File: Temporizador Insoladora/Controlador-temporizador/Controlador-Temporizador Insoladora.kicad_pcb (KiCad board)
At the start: 2 copper layers, 170.2 x 96.5 mm, 72 parts, among them P1 ICSP, P2 CONN_01X03, P3 CARGA, P4 TRANSF, P5 VAC, P7 CONN_02X08, Q1 BC548, Q2 BC548, Q3 BC548, Q4 BC548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

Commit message: Acomodando el controlador
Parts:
- P2: value CONN_01X03 -> VAC12V
- moved D2 161.8 mm to (48.3, 69.8)
- moved D3 161.8 mm to (48.3, 64.8)
- moved P4 157.3 mm to (199.4, 87.6), turned to 270 degrees
- moved P5 145.4 mm to (199.4, 74.9), turned to 270 degrees
- moved P2 131.4 mm to (64.8, 73.7)
- moved F1 130.1 mm to (186.7, 77.5), turned to 90 degrees
- moved VR1 122.3 mm to (193.0, 82.5), turned to 90 degrees
- moved R10 76.0 mm to (52.1, 123.2)
- moved R11 76.0 mm to (50.8, 128.3)
- moved P7 71.1 mm to (134.6, 147.3), turned to 180 degrees
- moved Q6 69.1 mm to (109.2, 141.0), turned to 90 degrees
- moved R29 64.3 mm to (105.4, 134.6), turned to 90 degrees
- moved Q3 64.3 mm to (143.5, 139.7), turned to 90 degrees
- moved Q5 64.2 mm to (118.1, 141.0), turned to 90 degrees
- moved R15 62.6 mm to (151.1, 86.4), turned to 90 degrees
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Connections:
- P1 pad 6: Net-(P1-Pad6) -> (no net)
- P5 pad 2: Earth -> (no net)
- P7 pad 11: Net-(P7-Pad11) -> (no net)
- P7 pad 5: Net-(P7-Pad5) -> (no net)
- P7 pad 7: Net-(P7-Pad7) -> (no net)
- P7 pad 9: Net-(P7-Pad9) -> (no net)
- U2 pad 10: Net-(U2-Pad10) -> (no net)
- U2 pad 2: Net-(U2-Pad2) -> (no net)
- U2 pad 24: Net-(U2-Pad24) -> (no net)
- U2 pad 25: Net-(U2-Pad25) -> (no net)
- U2 pad 26: Net-(U2-Pad26) -> (no net)
- U2 pad 3: Net-(U2-Pad3) -> (no net)
- U2 pad 34: Net-(U2-Pad34) -> (no net)
- U2 pad 4: Net-(U2-Pad4) -> (no net)
- U2 pad 5: Net-(U2-Pad5) -> (no net)
- U2 pad 6: Net-(U2-Pad6) -> (no net)
- U2 pad 7: Net-(U2-Pad7) -> (no net)
- U2 pad 8: Net-(U2-Pad8) -> (no net)
- U2 pad 9: Net-(U2-Pad9) -> (no net)
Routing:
- net Net-(C13-Pad2): track 0.00 -> 48.2 mm
- net Net-(P3-Pad2): track 0.00 -> 36.4 mm
- net Net-(F1-Pad1): track 0.00 -> 34.8 mm
- net Net-(R19-Pad1): track 0.00 -> 16.6 mm
- net Net-(F1-Pad2): track 0.00 -> 15.2 mm
- net /D: track 22.1 -> 8.89 mm
- net SEGUKC: track 10.5 -> 0.00 mm
- net Net-(Q1-Pad2): track 0.00 -> 8.67 mm
- net Net-(R15-Pad1): track 0.00 -> 5.68 mm
- net Net-(R18-Pad2): track 0.00 -> 5.16 mm
- net SEGDKC: track 4.86 -> 0.00 mm
- net Net-(Q1-Pad1): track 0.00 -> 3.81 mm
- net Net-(Q5-Pad2): track 3.81 -> 0.00 mm
- net Net-(C13-Pad1): track 0.00 -> 3.59 mm
- net /E: track 6.35 -> 8.89 mm
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
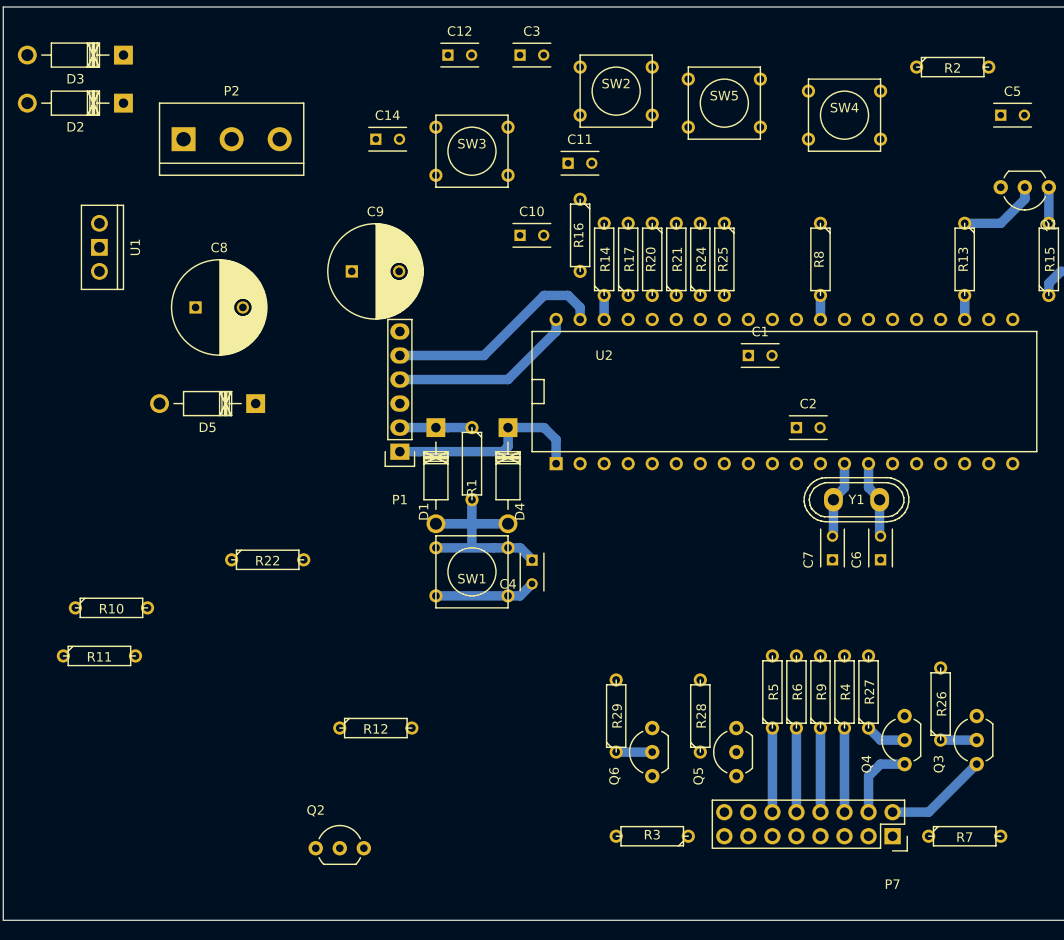
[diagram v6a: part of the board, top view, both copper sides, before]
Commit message: Ruteando controlador
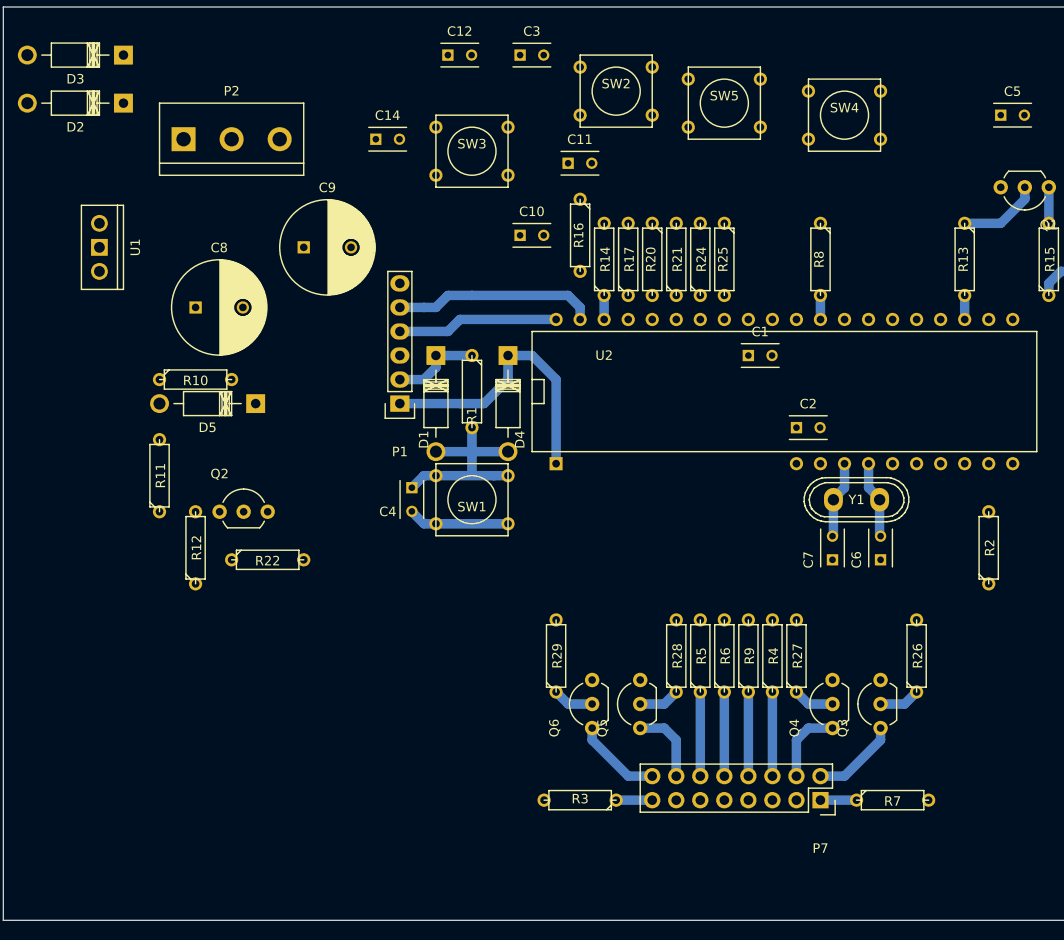
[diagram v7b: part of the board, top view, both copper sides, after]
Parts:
- moved R2 50.9 mm to (144.8, 116.8), turned to 90 degrees
- moved Q2 37.0 mm to (63.5, 113.0)
- moved R12 26.9 mm to (61.0, 116.8), turned to 90 degrees
- moved R10 25.7 mm to (61.0, 99.1)
- moved R11 20.1 mm to (57.1, 109.2), turned to 90 degrees
- moved C4 14.8 mm to (83.8, 110.5)
- moved Q5 11.4 mm to (108.0, 135.9)
- moved Q3 10.9 mm to (133.3, 135.9)
- moved R29 8.98 mm to (99.1, 128.3)
- moved R27 8.52 mm to (124.5, 128.3)
- moved P7 8.52 mm to (127.0, 143.5)
- moved R3 8.52 mm to (101.6, 143.5)
- moved R5 8.52 mm to (114.3, 128.3)
- moved R7 8.52 mm to (134.6, 143.5)
- moved R9 8.52 mm to (119.4, 128.3)
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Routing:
- net SEGUKC: track 0.00 -> 9.20 mm
- net ~MCLR~/VPP: track 21.8 -> 30.0 mm
- net SEGDKC: track 0.00 -> 8.15 mm
- net Net-(Q5-Pad2): track 0.00 -> 4.34 mm
- net /F: track 0.00 -> 3.81 mm
- net /B: track 0.00 -> 3.81 mm
- net PGD: track 19.9 -> 17.0 mm
- net PGC: track 23.5 -> 21.4 mm
- net VCC: track 7.62 -> 9.42 mm
- net MINDKC: track 11.0 -> 9.20 mm
- net Net-(Q6-Pad2): track 3.81 -> 4.34 mm
- net Net-(Q3-Pad2): track 3.81 -> 4.34 mm

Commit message: Ruteando Controlador
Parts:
- moved R22 63.1 mm to (120.7, 82.5), turned to 270 degrees
- moved R8 56.4 mm to (134.6, 142.2), turned to 0 degrees
- moved C12 37.4 mm to (118.1, 86.4), turned to 90 degrees
- moved R3 33.6 mm to (134.6, 149.9), turned to 0 degrees
- moved C14 33.0 mm to (110.5, 86.4), turned to 90 degrees
- moved R2 30.9 mm to (134.6, 146.1), turned to 0 degrees
- moved Q2 24.1 mm to (86.4, 120.7)
- moved U1 23.4 mm to (73.7, 80.0), turned to 90 degrees
- moved P2 22.7 mm to (44.5, 83.8), turned to 90 degrees
- moved C3 21.6 mm to (80.0, 80.0), turned to 90 degrees
- moved C8 20.9 mm to (66.0, 71.1)
- moved R12 20.8 mm to (77.5, 104.1), turned to 270 degrees
- moved D2 20.5 mm to (55.9, 88.9)
- moved D5 18.2 mm to (66.0, 83.8)
- moved SW3 17.8 mm to (108.0, 73.7)
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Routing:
- net VCC: track 9.42 -> 102.9 mm
- net GND: track 10.7 -> 53.5 mm
- net /B: track 3.81 -> 27.8 mm
- net /A: track 0.00 -> 23.0 mm
- net GPI1: track 0.00 -> 15.5 mm
- net INICIAR/PARAR: track 0.00 -> 12.0 mm
- net BAJAR: track 0.00 -> 11.4 mm
- net Net-(R21-Pad2): track 0.00 -> 10.7 mm
- net SUBIR: track 2.54 -> 13.0 mm
- net Net-(R24-Pad2): track 0.00 -> 10.2 mm
- net Net-(R17-Pad2): track 0.00 -> 10.2 mm
- net Net-(R14-Pad2): track 0.00 -> 10.2 mm
- net /G: track 0.00 -> 9.42 mm
- net Net-(Q1-Pad2): track 8.67 -> 3.81 mm
- net Net-(Q1-Pad1): track 3.81 -> 6.35 mm
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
